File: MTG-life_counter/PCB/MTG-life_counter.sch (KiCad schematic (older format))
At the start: 33 parts, among them J2 AVR-ISP-6, Q1 IRLML6244, Q2 IRLML6244, Q4 Si2301DS, Q5 Si2301DS, U2 AT90S4433-8P, U3 HDSP-H101, U4 HDSP-H101, Y1 8 MHz

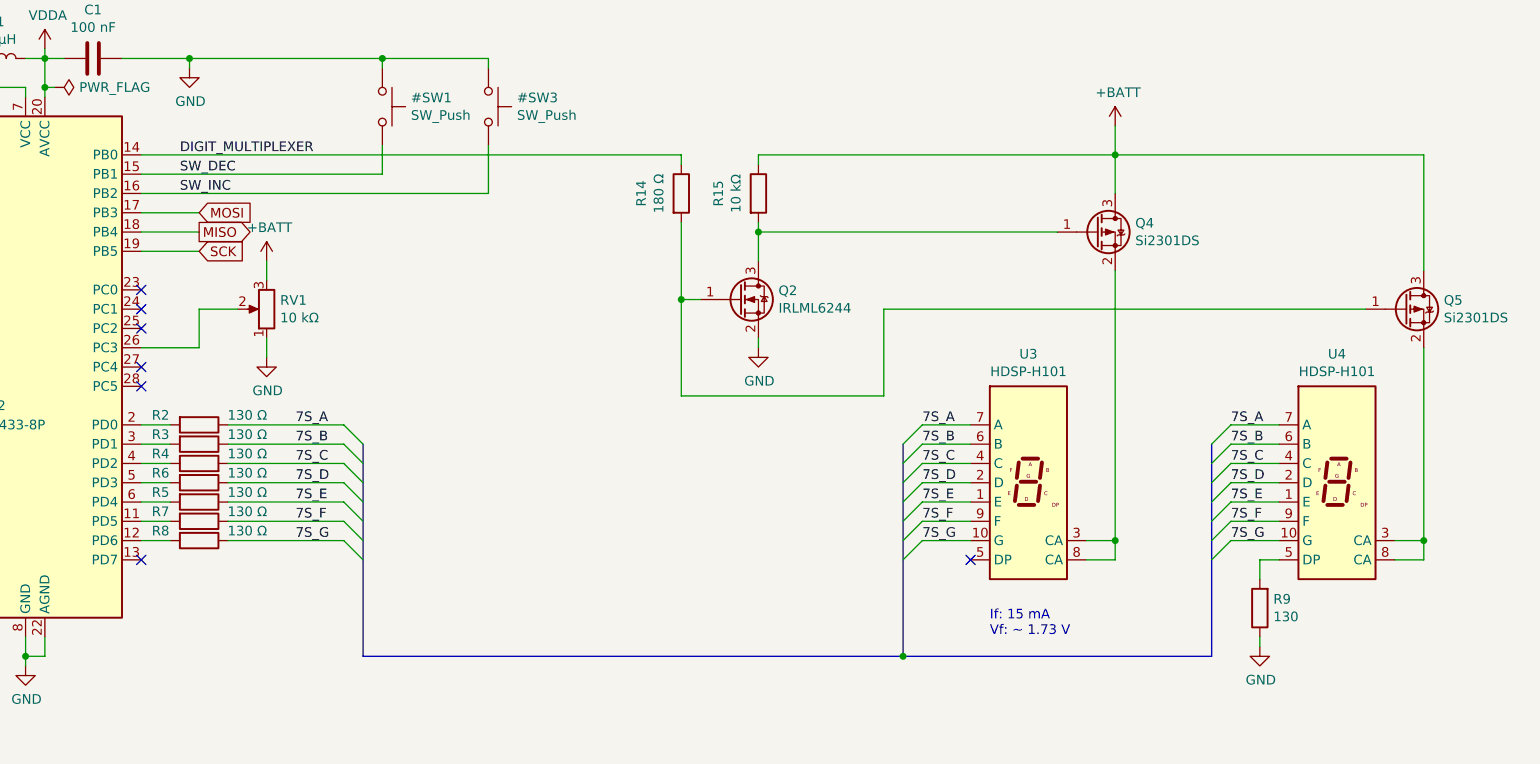
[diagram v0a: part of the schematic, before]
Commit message: Use a net tie for combining MOSI/MISO & DIGIT_X_ENABLE.
MOSI/MISO are used for programming, while the DIGIT_X_ENABLE lines enable the corresponding display digit.

That's pretty much it for the schematic. Finally.
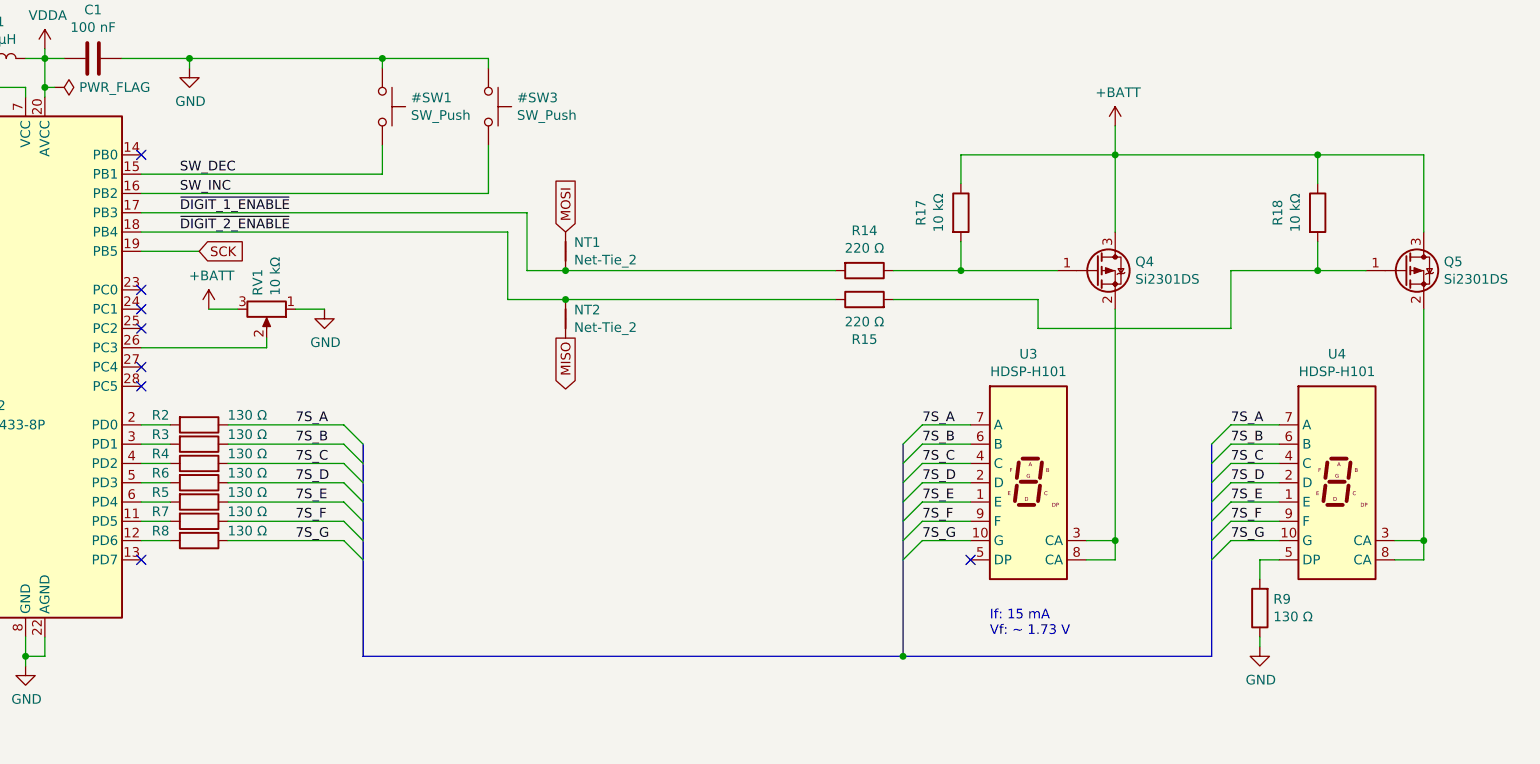
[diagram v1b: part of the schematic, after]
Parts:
- removed Q2: IRLML6244, Package_TO_SOT_SMD:SOT-23_Handsoldering, symbol Device:Q_NMOS_GSD
- added NT1, NT2: Net-Tie_2, NetTie:NetTie-2_SMD_Pad0.5mm, symbol Device:Net-Tie_2
- added R15: 220 Ω, Resistor_SMD:R_0805_2012Metric_Pad1.20x1.40mm_HandSolder, symbol Device:R
- added R18: 10 kΩ, Resistor_SMD:R_0805_2012Metric_Pad1.20x1.40mm_HandSolder, symbol Device:R
- R14: value 180 Ω -> 220 Ω
- R9: value 130 -> 130 Ω
- RV1: footprint (none) -> Potentiometer_THT:Potentiometer_Piher_PT-10-H01_Horizontal
- renumbered R15 to R17
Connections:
- net +BATT: now also R18.1
- net MISO: now also NT2.2; no longer U2.18 (PB4)
- net MOSI: now also NT1.1; no longer U2.17 (PB3)
- net at Q4.1 (G), R17.2: now also R14.1
- net at Q5.1 (G): now also R15.2, R18.2; no longer R14.2
- net DIGIT_MULTIPLEXER: no longer names the net of U2.14 (PB0)
- net DIGIT_MULTIPLEXER: no longer R14.1
- new net ~DIGIT_1_ENABLE: NT1.2, R14.2, U2.17 (PB3)
- new net ~DIGIT_2_ENABLE: NT2.1, R15.1, U2.18 (PB4)
- no-connect marks 7 -> 8
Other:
- moved on the sheet: Q4, Q5, R17, RV1
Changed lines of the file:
@@
 P 9900 4000
 F 0 "R9" H 9830 3954 50  0000 R CNN
-F 1 "130" H 9830 4045 50  0000 R CNN
+F 1 "130 Ω" H 9830 4045 50  0000 R CNN
 F 2 "Resistor_SMD:R_0805_2012Metric_Pad1.20x1.40mm_HandSolder" V 9830 4000 50  0001 C CNN
 F 3 "~" H 9900 4000 50  0001 C CNN
@@
 Wire Wire Line
 	5900 1850 5900 1600
-Wire Wire Line
-	4100 2650 4400 2650
-Wire Wire Line
-	4750 2300 4750 2200
-Wire Wire Line
-	4750 2600 4750 2700
-$Comp
-L power:GND #PWR011
-U 1 1 6146287A
-P 4750 2700
-F 0 "#PWR011" H 4750 2450 50  0001 C CNN
-F 1 "GND" H 4755 2527 50  0000 C CNN
-F 2 "" H 4750 2700 50  0001 C CNN
-F 3 "" H 4750 2700 50  0001 C CNN
-	1    4750 2700
-	1    0    0    -1
-$EndComp
-$Comp
-L Device:R_POT RV1
-U 1 1 61456388
-P 4750 2450
-F 0 "RV1" H 4680 2404 50  0000 R CNN
-F 1 "10 kΩ" H 4680 2495 50  0000 R CNN
-F 2 "" H 4750 2450 50  0001 C CNN
-F 3 "~" H 4750 2450 50  0001 C CNN
-	1    4750 2450
-	-1   0    0    1
-$EndComp
-Wire Wire Line
-	4400 2650 4400 2450
-Wire Wire Line
-	4400 2450 4600 2450
 NoConn ~ 4100 2850
 NoConn ~ 4100 2750
@@
 Text GLabel 5500 6950 0    50   Output ~ 0
 ~RESET
-Text GLabel 4400 2050 2    50   Output ~ 0
+Text GLabel 6300 2600 3    50   Output ~ 0
 MISO
-Text GLabel 4400 1950 2    50   Input ~ 0
-MOSI
 Text GLabel 4400 2150 2    50   Input ~ 0
 SCK
@@
 Wire Wire Line
 	4400 2150 4100 2150
-Wire Wire Line
-	4400 1950 4100 1950
-Wire Wire Line
-	4100 2050 4400 2050
 $Sheet
 S 850  5700 1350 900
@@
 L Device:Q_PMOS_GSD Q5
 U 1 1 61A59774
-P 10650 2450
-F 0 "Q5" H 10854 2496 50  0000 L CNN
-F 1 "Si2301DS" H 10854 2405 50  0000 L CNN
-F 2 "Package_TO_SOT_SMD:SOT-23_Handsoldering" H 10850 2550 50  0001 C CNN
-F 3 "~" H 10650 2450 50  0001 C CNN
-	1    10650 2450
+P 10650 2250
+F 0 "Q5" H 10854 2296 50  0000 L CNN
+F 1 "Si2301DS" H 10854 2205 50  0000 L CNN
+F 2 "Package_TO_SOT_SMD:SOT-23_Handsoldering" H 10850 2350 50  0001 C CNN
+F 3 "~" H 10650 2250 50  0001 C CNN
+	1    10650 2250
 	1    0    0    -1
 $EndComp
@@
 Connection ~ 9150 3650
 Wire Wire Line
-	9150 3650 9150 2250
+	9150 3650 9150 2450
 Wire Wire Line
 	10600 3750 10750 3750
@@
 Connection ~ 10750 3650
 Wire Wire Line
-	10750 3650 10750 2650
+	10750 3650 10750 2450
 Wire Wire Line
 	9150 1500 9150 1650
 Wire Wire Line
-	10750 1650 10750 2250
+	10750 1650 10750 2050
 Connection ~ 9150 1650
 Wire Wire Line
-	9150 1650 9150 1850
-$Comp
-L Device:Q_NMOS_GSD Q2
-U 1 1 61ADE8BB
-P 7200 2400
-F 0 "Q2" H 7404 2446 50  0000 L CNN
-F 1 "IRLML6244" H 7404 2355 50  0000 L CNN
-F 2 "Package_TO_SOT_SMD:SOT-23_Handsoldering" H 7400 2500 50  0001 C CNN
-F 3 "~" H 7200 2400 50  0001 C CNN
-	1    7200 2400
-	1    0    0    -1
-$EndComp
-$Comp
-L power:GND #PWR016
-U 1 1 61ADF816
-P 7300 2650
-F 0 "#PWR016" H 7300 2400 50  0001 C CNN
-F 1 "GND" H 7305 2477 50  0000 C CNN
-F 2 "" H 7300 2650 50  0001 C CNN
-F 3 "" H 7300 2650 50  0001 C CNN
-	1    7300 2650
-	1    0    0    -1
-$EndComp
-Wire Wire Line
-	7300 2650 7300 2600
-$Comp
-L Device:R R15
+	9150 1650 9150 2050
+$Comp
+L Device:R R17
 U 1 1 61B139BA
-P 7300 1850
-F 0 "R15" V 7093 1850 50  0000 C CNN
-F 1 "10 kΩ" V 7184 1850 50  0000 C CNN
-F 2 "Resistor_SMD:R_0805_2012Metric_Pad1.20x1.40mm_HandSolder" V 7230 1850 50  0001 C CNN
-F 3 "~" H 7300 1850 50  0001 C CNN
-	1    7300 1850
-	1    0    0    -1
-$EndComp
-Wire Wire Line
-	7300 1700 7300 1650
-Wire Wire Line
-	7300 1650 9150 1650
-$Comp
-L Device:R R14
-U 1 1 61B45BA3
-P 6900 1850
-F 0 "R14" V 6693 1850 50  0000 C CNN
-F 1 "180 Ω" V 6784 1850 50  0000 C CNN
-F 2 "Resistor_SMD:R_0805_2012Metric_Pad1.20x1.40mm_HandSolder" V 6830 1850 50  0001 C CNN
-F 3 "~" H 6900 1850 50  0001 C CNN
-	1    6900 1850
-	1    0    0    -1
-$EndComp
-Wire Wire Line
-	6900 2000 6900 2400
-Wire Wire Line
-	6900 2400 6900 2900
-Wire Wire Line
-	6900 2900 7950 2900
-Wire Wire Line
-	7950 2900 7950 2450
-Wire Wire Line
-	7950 2450 10450 2450
-Connection ~ 6900 2400
-Wire Wire Line
-	6900 2400 7000 2400
-Wire Wire Line
-	6900 1700 6900 1650
-Wire Wire Line
-	6900 1650 4100 1650
-Text Label 4300 1650 0    50   ~ 0
-DIGIT_MULTIPLEXER
-Wire Wire Line
-	9150 1650 10750 1650
+P 8350 1950
+F 0 "R17" V 8143 1950 50  0000 C CNN
+F 1 "10 kΩ" V 8234 1950 50  0000 C CNN
+F 2 "Resistor_SMD:R_0805_2012Metric_Pad1.20x1.40mm_HandSolder" V 8280 1950 50  0001 C CNN
+F 3 "~" H 8350 1950 50  0001 C CNN
+	1    8350 1950
+	1    0    0    -1
+$EndComp
+Wire Wire Line
+	8350 1800 8350 1650
+Wire Wire Line
+	8350 1650 9150 1650
+Wire Wire Line
+	9150 1650 10200 1650
 $Comp
 L Device:Q_PMOS_GSD Q4
 U 1 1 61A579B0
-P 9050 2050
-F 0 "Q4" H 9254 2096 50  0000 L CNN
-F 1 "Si2301DS" H 9254 2005 50  0000 L CNN
-F 2 "Package_TO_SOT_SMD:SOT-23_Handsoldering" H 9250 2150 50  0001 C CNN
-F 3 "~" H 9050 2050 50  0001 C CNN
-	1    9050 2050
-	1    0    0    -1
-$EndComp
-Wire Wire Line
-	7300 2000 7300 2050
-Wire Wire Line
-	8850 2050 7300 2050
-Connection ~ 7300 2050
-Wire Wire Line
-	7300 2050 7300 2200
+P 9050 2250
+F 0 "Q4" H 9254 2296 50  0000 L CNN
+F 1 "Si2301DS" H 9254 2205 50  0000 L CNN
+F 2 "Package_TO_SOT_SMD:SOT-23_Handsoldering" H 9250 2350 50  0001 C CNN
+F 3 "~" H 9050 2250 50  0001 C CNN
+	1    9050 2250
+	1    0    0    -1
+$EndComp
 NoConn ~ 4100 2450
 NoConn ~ 4100 2350
@@
 $EndComp
 $Comp
-L power:+BATT #PWR0102
-U 1 1 61C17C07
-P 4750 2200
-F 0 "#PWR0102" H 4750 2050 50  0001 C CNN
-F 1 "+BATT" H 4765 2373 50  0000 C CNN
-F 2 "" H 4750 2200 50  0001 C CNN
-F 3 "" H 4750 2200 50  0001 C CNN
-	1    4750 2200
-	1    0    0    -1
-$EndComp
-$Comp
 L power:+BATT #PWR0103
 U 1 1 61C18617
@@
 Wire Wire Line
 	6200 6200 6200 6350
+$Comp
+L Device:R R14
+U 1 1 61B08127
+P 7850 2250
+F 0 "R14" V 7643 2250 50  0000 C CNN
+F 1 "220 Ω" V 7734 2250 50  0000 C CNN
+F 2 "Resistor_SMD:R_0805_2012Metric_Pad1.20x1.40mm_HandSolder" V 7780 2250 50  0001 C CNN
+F 3 "~" H 7850 2250 50  0001 C CNN
+	1    7850 2250
+	0    1    1    0
+$EndComp
+$Comp
+L Device:R R15
+U 1 1 61B086B3
+P 7850 2400
+F 0 "R15" V 7643 2400 50  0000 C CNN
+F 1 "220 Ω" V 7734 2400 50  0000 C CNN
+F 2 "Resistor_SMD:R_0805_2012Metric_Pad1.20x1.40mm_HandSolder" V 7780 2400 50  0001 C CNN
+F 3 "~" H 7850 2400 50  0001 C CNN
+	1    7850 2400
+	0    -1   -1   0
+$EndComp
+NoConn ~ 4100 1650
+Wire Wire Line
+	8350 2100 8350 2250
+$Comp
+L Device:R R18
+U 1 1 61B3C230
+P 10200 1950
+F 0 "R18" V 9993 1950 50  0000 C CNN
+F 1 "10 kΩ" V 10084 1950 50  0000 C CNN
+F 2 "Resistor_SMD:R_0805_2012Metric_Pad1.20x1.40mm_HandSolder" V 10130 1950 50  0001 C CNN
+F 3 "~" H 10200 1950 50  0001 C CNN
+	1    10200 1950
+	1    0    0    -1
+$EndComp
+Wire Wire Line
+	10200 1800 10200 1650
+Connection ~ 10200 1650
+Wire Wire Line
+	10200 1650 10750 1650
+Wire Wire Line
+	10200 2100 10200 2250
+Wire Wire Line
+	10200 2250 10450 2250
+Wire Wire Line
+	8000 2250 8350 2250
+Wire Wire Line
+	8350 2250 8850 2250
+Connection ~ 8350 2250
+Connection ~ 10200 2250
+Wire Wire Line
+	7700 2250 6300 2250
+Wire Wire Line
+	6100 2250 6100 1950
+Wire Wire Line
+	6100 1950 4100 1950
+Text Label 4300 1950 0    50   ~ 0
+~DIGIT_1_ENABLE
+Text Label 4300 2050 0    50   ~ 0
+~DIGIT_2_ENABLE
+$Comp
+L Device:R_POT RV1
+U 1 1 61456388
+P 4750 2450
+F 0 "RV1" H 4680 2404 50  0000 R CNN
+F 1 "10 kΩ" H 4680 2495 50  0000 R CNN
+F 2 "Potentiometer_THT:Potentiometer_Piher_PT-10-H01_Horizontal" H 4750 2450 50  0001 C CNN
+F 3 "~" H 4750 2450 50  0001 C CNN
+	1    4750 2450
+	0    1    1    0
+$EndComp
+Wire Wire Line
+	8000 2400 8750 2400
+Wire Wire Line
+	8750 2400 8750 2550
+$Comp
+L power:+BATT #PWR0102
+U 1 1 61C17C07
+P 4450 2450
+F 0 "#PWR0102" H 4450 2300 50  0001 C CNN
+F 1 "+BATT" H 4465 2623 50  0000 C CNN
+F 2 "" H 4450 2450 50  0001 C CNN
+F 3 "" H 4450 2450 50  0001 C CNN
+	1    4450 2450
+	1    0    0    -1
+$EndComp
+$Comp
+L power:GND #PWR011
+U 1 1 6146287A
+P 5050 2450
+F 0 "#PWR011" H 5050 2200 50  0001 C CNN
+F 1 "GND" H 5055 2277 50  0000 C CNN
+F 2 "" H 5050 2450 50  0001 C CNN
+F 3 "" H 5050 2450 50  0001 C CNN
+	1    5050 2450
+	1    0    0    -1
+$EndComp
+Wire Wire Line
+	4900 2450 5050 2450
+Wire Wire Line
+	4450 2450 4600 2450
+Wire Wire Line
+	4750 2650 4750 2600
+Wire Wire Line
+	4100 2650 4750 2650
+Wire Wire Line
+	6000 2050 6000 2400
+Wire Wire Line
+	4100 2050 6000 2050
+Wire Wire Line
+	6000 2400 6300 2400
+Wire Wire Line
+	9750 2550 9750 2250
+Wire Wire Line
+	8750 2550 9750 2550
+Wire Wire Line
+	9750 2250 10200 2250
+Text GLabel 6300 2050 1    50   Input ~ 0
+MOSI
+$Comp
+L Device:Net-Tie_2 NT2
+U 1 1 61B04413
+P 6300 2500
+F 0 "NT2" V 6254 2544 50  0000 L CNN
+F 1 "Net-Tie_2" V 6345 2544 50  0000 L CNN
+F 2 "NetTie:NetTie-2_SMD_Pad0.5mm" H 6300 2500 50  0001 C CNN
+F 3 "~" H 6300 2500 50  0001 C CNN
+	1    6300 2500
+	0    1    1    0
+$EndComp
+Connection ~ 6300 2400
+Wire Wire Line
+	6300 2400 7700 2400
+$Comp
+L Device:Net-Tie_2 NT1
+U 1 1 61B2FD31
+P 6300 2150
+F 0 "NT1" V 6254 2194 50  0000 L CNN
+F 1 "Net-Tie_2" V 6345 2194 50  0000 L CNN
+F 2 "NetTie:NetTie-2_SMD_Pad0.5mm" H 6300 2150 50  0001 C CNN
+F 3 "~" H 6300 2150 50  0001 C CNN
+	1    6300 2150
+	0    1    1    0
+$EndComp
+Connection ~ 6300 2250
+Wire Wire Line
+	6300 2250 6100 2250
 Wire Bus Line
 	5250 3150 5250 4250

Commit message: Use better fitting footprints.
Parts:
- D2: footprint LED_THT:LED_D3.0mm -> LED_THT:LED_D3.0mm_Horizontal_O1.27mm_Z2.0mm
- H1, H2, H3, H4: footprint MountingHole:MountingHole_3.2mm_M3_Pad_Via -> mibe:SMTSO-M3
- Y1: footprint Crystal:Crystal_HC49-U_Horizontal -> Crystal:Crystal_HC49-4H_Vertical
- renumbered Q4 to Q2, Q5 to Q3
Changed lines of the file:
@@
 F 0 "Y1" V 2254 2081 50  0000 L CNN
 F 1 "8 MHz" V 2345 2081 50  0000 L CNN
-F 2 "Crystal:Crystal_HC49-U_Horizontal" H 2300 1950 50  0001 C CNN
+F 2 "Crystal:Crystal_HC49-4H_Vertical" H 2300 1950 50  0001 C CNN
 F 3 "~" H 2300 1950 50  0001 C CNN
 	1    2300 1950
@@
 F 0 "H1" H 7350 6149 50  0000 L CNN
 F 1 "MountingHole_Pad" H 7350 6058 50  0000 L CNN
-F 2 "MountingHole:MountingHole_3.2mm_M3_Pad_Via" H 7250 6100 50  0001 C CNN
+F 2 "mibe:SMTSO-M3" H 7250 6100 50  0001 C CNN
 F 3 "~" H 7250 6100 50  0001 C CNN
 	1    7250 6100
@@
 F 0 "H2" H 8300 6149 50  0000 L CNN
 F 1 "MountingHole_Pad" H 8300 6058 50  0000 L CNN
-F 2 "MountingHole:MountingHole_3.2mm_M3_Pad_Via" H 8200 6100 50  0001 C CNN
+F 2 "mibe:SMTSO-M3" H 8200 6100 50  0001 C CNN
 F 3 "~" H 8200 6100 50  0001 C CNN
 	1    8200 6100
@@
 F 0 "H3" H 9250 6149 50  0000 L CNN
 F 1 "MountingHole_Pad" H 9250 6058 50  0000 L CNN
-F 2 "MountingHole:MountingHole_3.2mm_M3_Pad_Via" H 9150 6100 50  0001 C CNN
+F 2 "mibe:SMTSO-M3" H 9150 6100 50  0001 C CNN
 F 3 "~" H 9150 6100 50  0001 C CNN
 	1    9150 6100
@@
 F 0 "H4" H 10200 6149 50  0000 L CNN
 F 1 "MountingHole_Pad" H 10200 6058 50  0000 L CNN
-F 2 "MountingHole:MountingHole_3.2mm_M3_Pad_Via" H 10100 6100 50  0001 C CNN
+F 2 "mibe:SMTSO-M3" H 10100 6100 50  0001 C CNN
 F 3 "~" H 10100 6100 50  0001 C CNN
 	1    10100 6100
@@
 F 0 "D2" H 3093 7067 50  0000 C CNN
 F 1 "LED red" H 3093 6976 50  0000 C CNN
-F 2 "LED_THT:LED_D3.0mm" H 3100 6850 50  0001 C CNN
+F 2 "LED_THT:LED_D3.0mm_Horizontal_O1.27mm_Z2.0mm" H 3100 6850 50  0001 C CNN
 F 3 "~" H 3100 6850 50  0001 C CNN
 F 4 "Vf 1.6 V; If 2 mA" H 3100 6850 50  0001 C CNN "Characteristics"
@@
 Low = Charging
 $Comp
-L Device:Q_PMOS_GSD Q5
+L Device:Q_PMOS_GSD Q3
 U 1 1 61A59774
 P 10650 2250
-F 0 "Q5" H 10854 2296 50  0000 L CNN
+F 0 "Q3" H 10854 2296 50  0000 L CNN
 F 1 "Si2301DS" H 10854 2205 50  0000 L CNN
 F 2 "Package_TO_SOT_SMD:SOT-23_Handsoldering" H 10850 2350 50  0001 C CNN
@@
 	9150 1650 10200 1650
 $Comp
-L Device:Q_PMOS_GSD Q4
+L Device:Q_PMOS_GSD Q2
 U 1 1 61A579B0
 P 9050 2250
-F 0 "Q4" H 9254 2296 50  0000 L CNN
+F 0 "Q2" H 9254 2296 50  0000 L CNN
 F 1 "Si2301DS" H 9254 2205 50  0000 L CNN
 F 2 "Package_TO_SOT_SMD:SOT-23_Handsoldering" H 9250 2350 50  0001 C CNN

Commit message: Add a decoupling cap to VCC of the microcontroller.
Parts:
- added C6: 100 nF, Capacitor_SMD:C_0805_2012Metric_Pad1.18x1.45mm_HandSolder, symbol Device:C
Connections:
- net +BATT: now also C6.1
- net GND: now also C6.2
- net XTAL2: now reaches C3.1, U2.10 (XTAL2), Y1.2
- net XTAL1: now reaches C2.1, U2.9 (XTAL1), Y1.1
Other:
- moved on the sheet: C2, C3
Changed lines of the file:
@@
 L Device:C C2
 U 1 1 6141DCBC
-P 1850 1800
-F 0 "C2" V 1598 1800 50  0000 C CNN
-F 1 "33 pF" V 1689 1800 50  0000 C CNN
-F 2 "Capacitor_SMD:C_1206_3216Metric_Pad1.42x1.75mm_HandSolder" H 1888 1650 50  0001 C CNN
-F 3 "~" H 1850 1800 50  0001 C CNN
-	1    1850 1800
+P 1600 1800
+F 0 "C2" V 1348 1800 50  0000 C CNN
+F 1 "33 pF" V 1439 1800 50  0000 C CNN
+F 2 "Capacitor_SMD:C_1206_3216Metric_Pad1.42x1.75mm_HandSolder" H 1638 1650 50  0001 C CNN
+F 3 "~" H 1600 1800 50  0001 C CNN
+	1    1600 1800
 	0    1    1    0
 $EndComp
@@
 L Device:C C3
 U 1 1 6141E339
-P 1850 2100
-F 0 "C3" V 2100 2100 50  0000 C CNN
-F 1 "33 pF" V 2000 2100 50  0000 C CNN
-F 2 "Capacitor_SMD:C_1206_3216Metric_Pad1.42x1.75mm_HandSolder" H 1888 1950 50  0001 C CNN
-F 3 "~" H 1850 2100 50  0001 C CNN
-	1    1850 2100
+P 1600 2100
+F 0 "C3" V 1850 2100 50  0000 C CNN
+F 1 "33 pF" V 1750 2100 50  0000 C CNN
+F 2 "Capacitor_SMD:C_1206_3216Metric_Pad1.42x1.75mm_HandSolder" H 1638 1950 50  0001 C CNN
+F 3 "~" H 1600 2100 50  0001 C CNN
+	1    1600 2100
 	0    1    1    0
 $EndComp
@@
 L power:GND #PWR03
 U 1 1 6141EB88
-P 1450 2150
-F 0 "#PWR03" H 1450 1900 50  0001 C CNN
-F 1 "GND" H 1455 1977 50  0000 C CNN
-F 2 "" H 1450 2150 50  0001 C CNN
-F 3 "" H 1450 2150 50  0001 C CNN
-	1    1450 2150
+P 1200 2150
+F 0 "#PWR03" H 1200 1900 50  0001 C CNN
+F 1 "GND" H 1205 1977 50  0000 C CNN
+F 2 "" H 1200 2150 50  0001 C CNN
+F 3 "" H 1200 2150 50  0001 C CNN
+	1    1200 2150
 	1    0    0    -1
 $EndComp
@@
 $EndComp
 Wire Wire Line
-	2000 2100 2300 2100
-Wire Wire Line
-	2300 1800 2000 1800
-Wire Wire Line
-	1700 2100 1450 2100
-Wire Wire Line
-	1450 2100 1450 1800
-Wire Wire Line
-	1450 1800 1700 1800
-Wire Wire Line
-	1450 2150 1450 2100
-Connection ~ 1450 2100
+	1450 2100 1200 2100
+Wire Wire Line
+	1200 2100 1200 1800
+Wire Wire Line
+	1200 1800 1450 1800
+Wire Wire Line
+	1200 2150 1200 2100
+Connection ~ 1200 2100
 Wire Wire Line
 	4000 1150 4350 1150
@@
 Wire Wire Line
 	2750 1850 2900 1850
-Connection ~ 2300 1800
 $Comp
 L mibe:HDSP-H101 U3
@@
 Wire Wire Line
 	2750 2050 2900 2050
-Connection ~ 2300 2100
 $Comp
 L Switch:SW_Push #SW3
@@
 Wire Wire Line
 	6300 2250 6100 2250
+$Comp
+L Device:C C6
+U 1 1 61E79B15
+P 2750 1150
+F 0 "C6" V 2498 1150 50  0000 C CNN
+F 1 "100 nF" V 2589 1150 50  0000 C CNN
+F 2 "Capacitor_SMD:C_0805_2012Metric_Pad1.18x1.45mm_HandSolder" H 2788 1000 50  0001 C CNN
+F 3 "~" H 2750 1150 50  0001 C CNN
+	1    2750 1150
+	0    1    1    0
+$EndComp
+$Comp
+L power:GND #PWR0104
+U 1 1 61EA9491
+P 2550 1200
+F 0 "#PWR0104" H 2550 950 50  0001 C CNN
+F 1 "GND" H 2555 1027 50  0000 C CNN
+F 2 "" H 2550 1200 50  0001 C CNN
+F 3 "" H 2550 1200 50  0001 C CNN
+	1    2550 1200
+	1    0    0    -1
+$EndComp
+Wire Wire Line
+	3050 1150 2900 1150
+Wire Wire Line
+	2600 1150 2550 1150
+Wire Wire Line
+	2550 1150 2550 1200
+Text Label 1850 1800 0    50   ~ 0
+XTAL1
+Text Label 1850 2100 0    50   ~ 0
+XTAL2
+Wire Wire Line
+	1750 2100 2300 2100
+Connection ~ 2300 2100
+Wire Wire Line
+	1750 1800 2300 1800
 Wire Bus Line
 	5250 3150 5250 4250
@@
 Wire Bus Line
 	9650 3150 9650 4250
+Connection ~ 2300 1800
 $EndSCHEMATC
